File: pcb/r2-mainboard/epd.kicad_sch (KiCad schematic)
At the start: 0 parts

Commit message: R2: port epd, epd_power and power_mon from R1
WP4. These three sheets are copied from pcb/mainboard/ rather than redrawn,
because the acceptance criterion is "is it the same as R1" -- copying keeps
every part, value, coordinate and wire, so the two can be diffed directly.
tools/port_r1.py does it and only ever reads R1.

Result: epd and epd_power are provably identical to R1. R1's netlist was
exported from a scratch copy and the partition of each sheet's pins into nets
compared with R2's, undoing the designator renames first: 49/49 and 44/44 net
groups, identical. power_mon differs in exactly four groups, all intended.

103 of 128 parts keep their exact R1 designator; only collisions are renamed,
+200 for R/C and +20 for U/L so the R1 number stays readable inside the new one.
Other transforms: global labels become hierarchical labels (they are different
nets in KiCad, so a mixed project would have failed to connect silently);
I2C1_* becomes *_AON; three transistor symbols moved library in KiCad 10;
SY8120 and MT9700 are lifted into r2.kicad_sym because they are not in
pcb_common at all -- in R1 they survive only as embedded definitions.

power_mon's two video-decoder channels are gone with the ADV7611, so three
shunts are repurposed without any topology change: U22 now measures the SoM's
input current, the always-on domain, and the frontlight from +VSYS. All three
INA3221s move to +3V3_AON -- on a switched rail their I2C pins would clamp the
always-on bus, and power-down IQ is 0.5 uA typ, so the always-on domain finally
becomes measurable.

Two open items closed by reading R1 properly:

- The EPD chain cannot run from +VSYS. LGS5145 is a buck with a 4.5 V minimum,
  used here as an inverting buck-boost; in steady state it sees ~25 V, but at
  startup the negative rail is at 0 V and 3.0 V from a flat cell will not start
  it. power.md §9 closed.
- Negative rails are measured by dividing between the rail and +3V3_DCDC, not
  to ground. Carried over unchanged, with a f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
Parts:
- added C147, C158, C159, C60, C61, C62, C63: 100nF/50V, Capacitor_SMD:C_0402_1005Metric, symbol Device:C
- added J3: FPC-05F-16PH20, footprints:Xunpu_FPC-05F-16PH20_1x16-1MP_P0.50mm_Horizontal, symbol Connector_Generic_MountingPin:Conn_01x16_MountingPin
- added J6: FPC-05F-50PH20, footprints:Xunpu_FPC-05F-50PH20_1x50-1MP_P0.50mm_Horizontal, symbol Connector_Generic_MountingPin:Conn_01x50_MountingPin
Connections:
- new net +3V3: C60.1, J6.45 (Pin_45), J6.6 (Pin_6)
- new net +5V2_FL: C147.1, J6.44 (Pin_44), J6.7 (Pin_7)
- new net +VGH: C62.1, J6.3 (Pin_3)
- new net +VP: C158.1, J6.49 (Pin_49)
- new net -VCOM: C61.1, J6.5 (Pin_5)
- new net -VGL: C63.1, J6.1 (Pin_1)
- new net -VN: C159.1, J6.47 (Pin_47)
- new net EPDC_CLKN: J3.2 (Pin_2)
- new net EPDC_CLKP: J3.3 (Pin_3)
- new net EPDC_D0N: J6.38 (Pin_38)
- new net EPDC_D0P: J6.39 (Pin_39)
- new net EPDC_D10N: J3.8 (Pin_8)
- new net EPDC_D10P: J3.9 (Pin_9)
- new net EPDC_D11N: J3.5 (Pin_5)
- new net EPDC_D11P: J3.6 (Pin_6)
- new net EPDC_D1N: J6.35 (Pin_35)
- new net EPDC_D1P: J6.36 (Pin_36)
- new net EPDC_D2N: J6.32 (Pin_32)
- new net EPDC_D2P: J6.33 (Pin_33)
- new net EPDC_D3N: J6.29 (Pin_29)
- new net EPDC_D3P: J6.30 (Pin_30)
- new net EPDC_D4N: J6.26 (Pin_26)
- new net EPDC_D4P: J6.27 (Pin_27)
- new net EPDC_D5N: J6.23 (Pin_23)
- new net EPDC_D5P: J6.24 (Pin_24)
- new net EPDC_D6N: J6.20 (Pin_20)
- new net EPDC_D6P: J6.21 (Pin_21)
- new net EPDC_D7N: J6.17 (Pin_17)
- new net EPDC_D7P: J6.18 (Pin_18)
- new net EPDC_D8N: J3.14 (Pin_14)
- new net EPDC_D8P: J3.15 (Pin_15)
- new net EPDC_D9N: J3.11 (Pin_11)
- new net EPDC_D9P: J3.12 (Pin_12)
- new net EPDC_GDCLK: J6.13 (Pin_13)
- new net EPDC_GDOE: J6.11 (Pin_11)
- new net EPDC_GDSP: J6.12 (Pin_12)
- new net EPDC_SDCE0: J6.10 (Pin_10)
- new net EPDC_SDLE: J6.9 (Pin_9)
- new net EPDC_SDOE: J6.8 (Pin_8)
- new net EPDC_SE_CLK: J6.15 (Pin_15)
- new net FL_EN: J6.43 (Pin_43)
- new net FL_PWM1: J6.41 (Pin_41)
- new net FL_PWM2: J6.42 (Pin_42)
- new net GND: C147.2, C158.2, C159.2, C60.2, C61.2, C62.2, C63.2, J3.1 (Pin_1), J3.10 (Pin_10), J3.13 (Pin_13), J3.16 (Pin_16), J3.4 (Pin_4), J3.7 (Pin_7), J3.MP (MountPin), J6.14 (Pin_14), J6.16 (Pin_16), J6.19 (Pin_19), J6.22 (Pin_22), J6.25 (Pin_25), J6.28 (Pin_28), J6.31 (Pin_31), J6.34 (Pin_34), J6.37 (Pin_37), J6.40 (Pin_40), J6.MP (MountPin)
- no-connect marks 0 -> 5
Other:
- note added: "SE_D0"
- note added: "SE_D1"
- note added: "SE_D10"
- note added: "SE_D11"
- note added: "SE_D12"
- note added: "SE_D13"
- note added: "SE_D14"
- note added: "SE_D15"
- note added: "SE_D2"
- note added: "SE_D3"
- note added: "SE_D4"
- note added: "SE_D5"
- note added: "SE_D6"
- note added: "SE_D7"
- note added: "SE_D8"
- note added: "SE_D9"
- company: (none) -> Copyright 2025 Modos Tech Inc

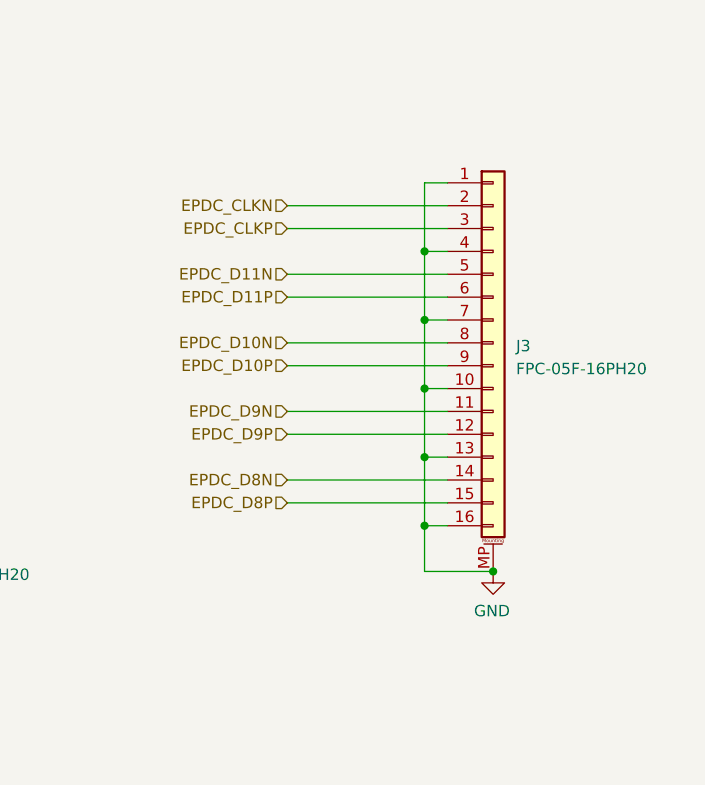
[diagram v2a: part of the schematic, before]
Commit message: R2: WP5 review answer 2 -- J3 is deleted, and with it ten dead nets
Owner's decision, manual-analysis/Analysis_fpga.md: "Yes, delete J3 connector."

J3 was the 16-pin panel connector. It carried nothing but EPDC_D8-D11 (eight
nets), EPDC_CLKP/CLKN and six grounds, and check_ucf.py had already shown that
no LOC line in Caster's constraint.ucf assigns any of the ten -- EPD_SD is 16
bits in every build variant and the UCF maps those 16 to panel pairs D0-D7, and
there is no EPD_CLK port in top.v at all. So this is not an unpopulated option;
nothing in the gateware could drive it.

Why it existed upstream, which the owner also asked: Glider is a general-purpose
EPD monitor. README "Screen Adapters" -- "A single 50pin connector is enough for
8/16-bit screens, the 16 pin connector additionally adds support for LVDS
screens and 32-bit/64-bit screens." In the screen list every MiniLVDS panel is
8" 1920x1440 or larger; every 6" 1448x1072 panel is TTL on 34 pins. R2 is a 6"
reader, so J3 is the large-panel option and J6 alone is the reader's connector.

tools/patch_drop_j3.py does it surgically -- both sheets are frozen. On epd:
J3, #PWR0201, ten hierarchical labels, ten signal wires, the thirteen-wire
ground comb and its six junctions. On fpga_io: ten labels and wires, and ten
no-connect flags on C7 A7 B8 A8 C9 A9 E7 E8 D8 C8. port_r1.py keeps the ten
names in HIER so a --force re-port still reproduces R1, and subtracts a new
DEAD_ON_R2 set from the sheet-pin list instead.

Verified: netlist before/after is 351 nets either way -- exactly the ten dead
nets gone, exactly seven J3 nodes off GND, ten new one-pin unconnected- nets on
the expected balls, and every other net byte-identical. check_ucf.py still 113
constrained balls / 0 failures, and its "reserved but not driven" list falls
from 11 balls to 1 (EPD_THROT). ERC unchanged at 105 excluding library links.
Both pages and the root rendered and read.

The r2.kicad_sch diff is large because removing ten sheet pins moves every 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
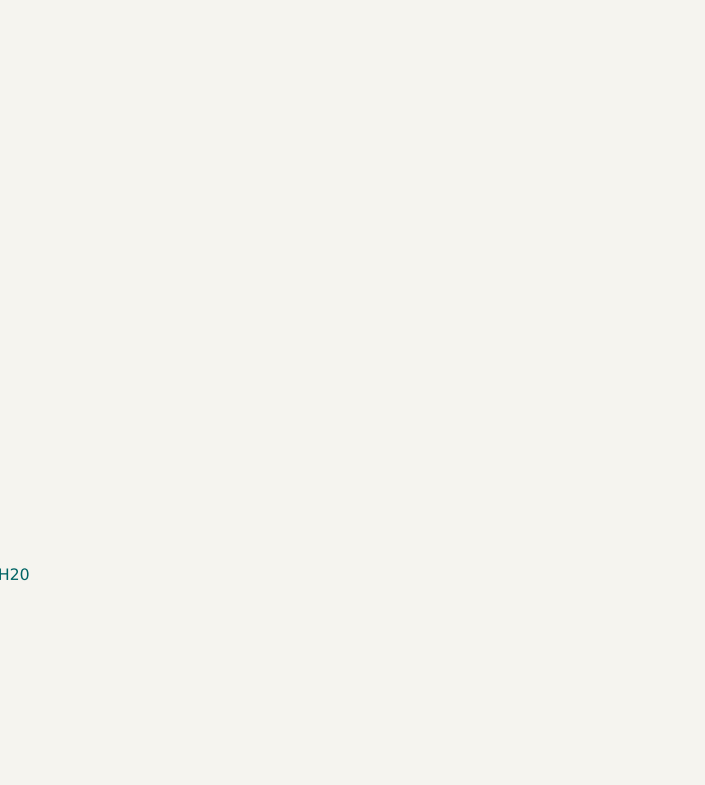
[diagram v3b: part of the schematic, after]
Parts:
- removed J3: FPC-05F-16PH20, footprints:Xunpu_FPC-05F-16PH20_1x16-1MP_P0.50mm_Horizontal, symbol Connector_Generic_MountingPin:Conn_01x16_MountingPin

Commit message: R2: MPNs into the schematic -- and five caps carry the wrong part number
Sourcing data lived in docs/*.md, not in the schematic, so the BOM the
fab would read had 3 of 96 lines with an MPN. Resolved every LCSC code
already on the board against LCSC's own catalogue and wrote MPN +
Manufacturer back: 53 -> 60 lines, 218 components. Added LCSC codes for
L10-L13, U42 and J22/J23 from the per-sheet docs.

Verified before writing: 321 refs and 519 nets identical before and
after, no duplicated properties, pre-existing MPNs untouched.

Cross-checking each passive value against the part its LCSC code
actually names found five wrong ones, all of them the ADC sense-divider
filter caps on power_mon:

  C91                 1nF/50V  carries C131394  = 100 nF
  C163 C164 C168 C169 1nF/25V  carries C6119801 = 470 nF

Left unwritten rather than cementing the error. C1523 (0402B102K500NT,
1 nF 50 V X7R 0402, JLC Basic, 5.3 M stock) covers both positions.

Also held back: U41, whose C39313 is XC6SLX16-**2**FTG256C while
fpga.md specifies the -3 speed grade.

frontlight.md cites C1848394 as the FPC connector on J22/J23; that code
is TPS22914BYFPR. The 6-pin sibling of J24's C5213749 is C5213748.

Co-Authored-By: Claude Opus 5 <noreply@anthropic.com>
Claude-Session: https://claude.ai/code/session_01MnesETWABbVdbcVnCKfKVs
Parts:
- C147, C158, C159, C60, C61, C62, C63: MPN (none) -> CC0402KRX7R9BB104; Manufacturer (none) -> YAGEO
- J6: MPN (none) -> FPC-05F-50PH20; Manufacturer (none) -> XUNPU
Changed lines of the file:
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@@
+			)
+		)
+		(property "Manufacturer" "YAGEO" (at 0 0 0)
+			(effects
+				(font
+					(size 1.27 1.27)
+				)
+				(hide yes)
+			)
+		)
+		(property "MPN" "CC0402KRX7R9BB104" (at 0 0 0)
+			(effects
+				(font
+					(size 1.27 1.27)
+				)
+				(hide yes)
 			)
 		)
@@
 			)
 		)
+		(property "Manufacturer" "YAGEO" (at 0 0 0)
+			(effects
+				(font
+					(size 1.27 1.27)
+				)
+				(hide yes)
+			)
+		)
+		(property "MPN" "CC0402KRX7R9BB104" (at 0 0 0)
+			(effects
+				(font
+					(size 1.27 1.27)
+				)
+				(hide yes)
+			)
+		)
 		(pin "1"
 		)
@@
 			)
 		)
+		(property "Manufacturer" "YAGEO" (at 0 0 0)
+			(effects
+				(font
+					(size 1.27 1.27)
+				)
+				(hide yes)
+			)
+		)
+		(property "MPN" "CC0402KRX7R9BB104" (at 0 0 0)
+			(effects
+				(font
+					(size 1.27 1.27)
+				)
+				(hide yes)
+			)
+		)
 		(pin "1"
 		)
@@
 			)
 		)
+		(property "Manufacturer" "XUNPU" (at 0 0 0)
+			(effects
+				(font
+					(size 1.27 1.27)
+				)
+				(hide yes)
+			)
+		)
+		(property "MPN" "FPC-05F-50PH20" (at 0 0 0)
+			(effects
+				(font
+					(size 1.27 1.27)
+				)
+				(hide yes)
+			)
+		)
 		(pin "1"
 		)
@@
 			)
 		)
+		(property "Manufacturer" "YAGEO" (at 0 0 0)
+			(effects
+				(font
+					(size 1.27 1.27)
+				)
+				(hide yes)
+			)
+		)
+		(property "MPN" "CC0402KRX7R9BB104" (at 0 0 0)
+			(effects
+				(font
+					(size 1.27 1.27)
+				)
+				(hide yes)
+			)
+		)
 		(pin "1"
 		)
@@
 			)
 		)
+		(property "Manufacturer" "YAGEO" (at 0 0 0)
+			(effects
+				(font
+					(size 1.27 1.27)
+				)
+				(hide yes)
+			)
+		)
+		(property "MPN" "CC0402KRX7R9BB104" (at 0 0 0)
+			(effects
+				(font
+					(size 1.27 1.27)
+				)
+				(hide yes)
+			)
+		)
 		(pin "1"
 		)
@@
 			)
 		)
+		(property "Manufacturer" "YAGEO" (at 0 0 0)
+			(effects
+				(font
+					(size 1.27 1.27)
+				)
+				(hide yes)
+			)
+		)
+		(property "MPN" "CC0402KRX7R9BB104" (at 0 0 0)
+			(effects
+				(font
+					(size 1.27 1.27)
+				)
+				(hide yes)
+			)
+		)
 		(pin "1"
 		)
@@
 			)
 		)
+		(property "Manufacturer" "YAGEO" (at 0 0 0)
+			(effects
+				(font
+					(size 1.27 1.27)
+				)
+				(hide yes)
+			)
+		)
+		(property "MPN" "CC0402KRX7R9BB104" (at 0 0 0)
+			(effects
+				(font
+					(size 1.27 1.27)
+				)
+				(hide yes)
+			)
+		)
